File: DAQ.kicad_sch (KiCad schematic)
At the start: 6 parts, among them IC1 ABX00053, IC2 TEENSY_4.1

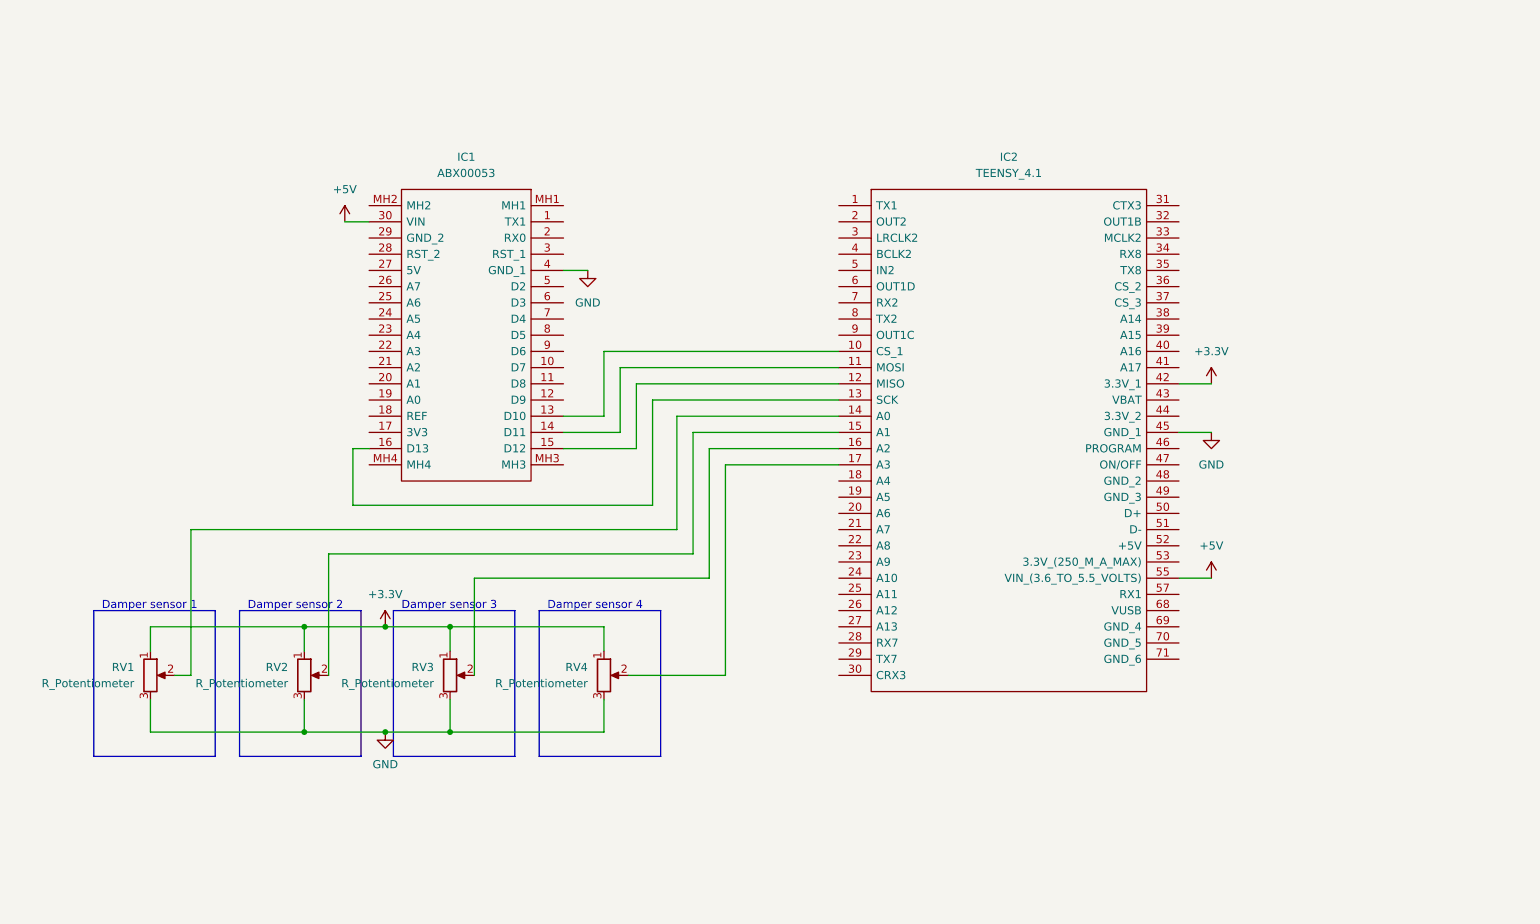
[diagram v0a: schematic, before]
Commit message: added wheel speed sensors connection
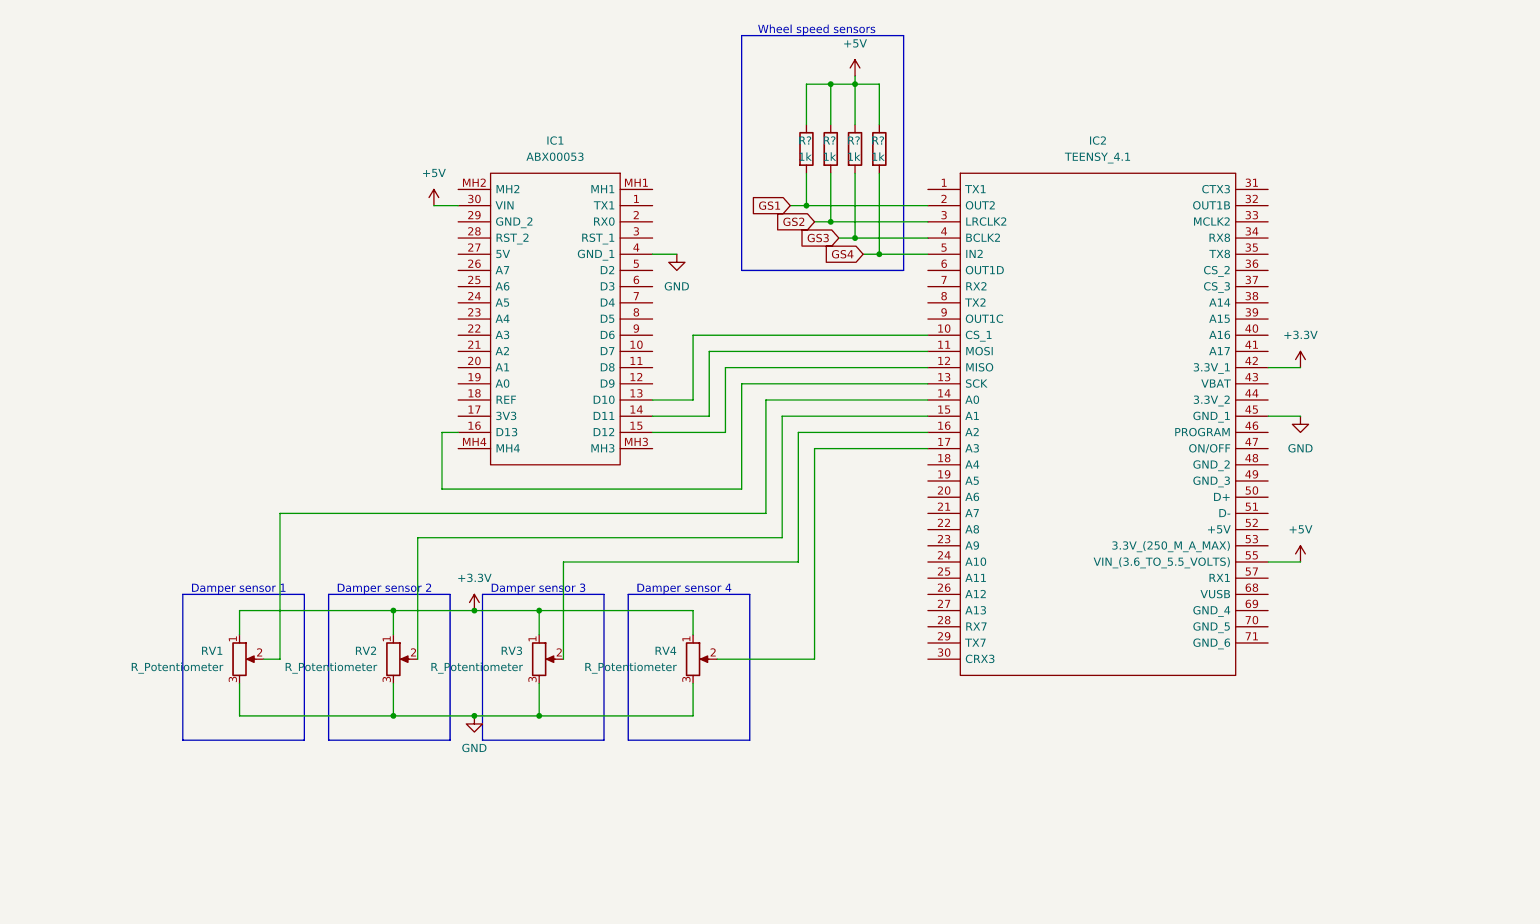
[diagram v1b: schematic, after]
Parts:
- added R? (x4): 1k, symbol Device:R
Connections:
- net +5V: now also R?.1, R?.1, R?.1, R?.1
- net GS1: now reaches IC2.2 (OUT2)
- net GS1: now also R?.2
- net GS2: now reaches IC2.3 (LRCLK2)
- net GS2: now also R?.2
- net GS3: now reaches IC2.4 (BCLK2)
- net GS3: now also R?.2
- net GS4: now reaches IC2.5 (IN2)
- net GS4: now also R?.2
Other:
- note added: "Wheel speed sensors"
- moved on the sheet: IC1, IC2, RV1, RV2, RV3, RV4

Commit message: added battery voltage sensor and steering wheel sensor
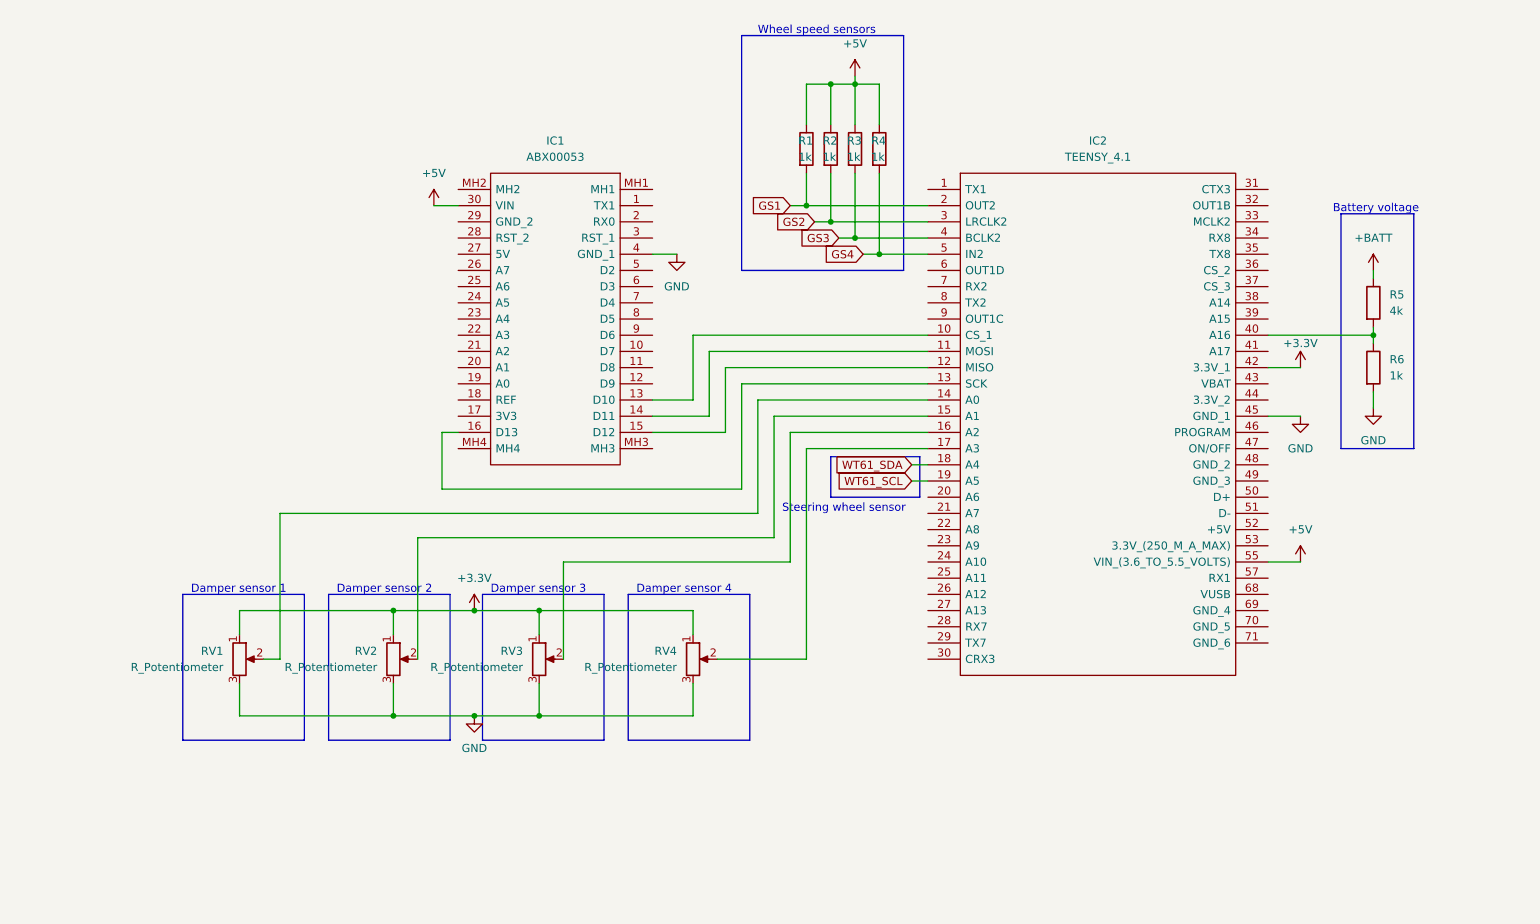
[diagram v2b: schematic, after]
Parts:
- added R5: 4k, symbol Device:R
- added R6: 1k, symbol Device:R
- gave numbers to parts that had none: 4
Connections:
- net GND: now also R6.2
- net WT61_SDA: now reaches IC2.18 (A4)
- net WT61_SCL: now reaches IC2.19 (A5)
- net at IC2.40 (A16): now also R5.2, R6.1
- new net +BATT: R5.1
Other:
- note added: "Battery voltage"
- note added: "Steering wheel sensor"

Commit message: new sensors
zener diode to hall effect input; coin cell for teensy RTC
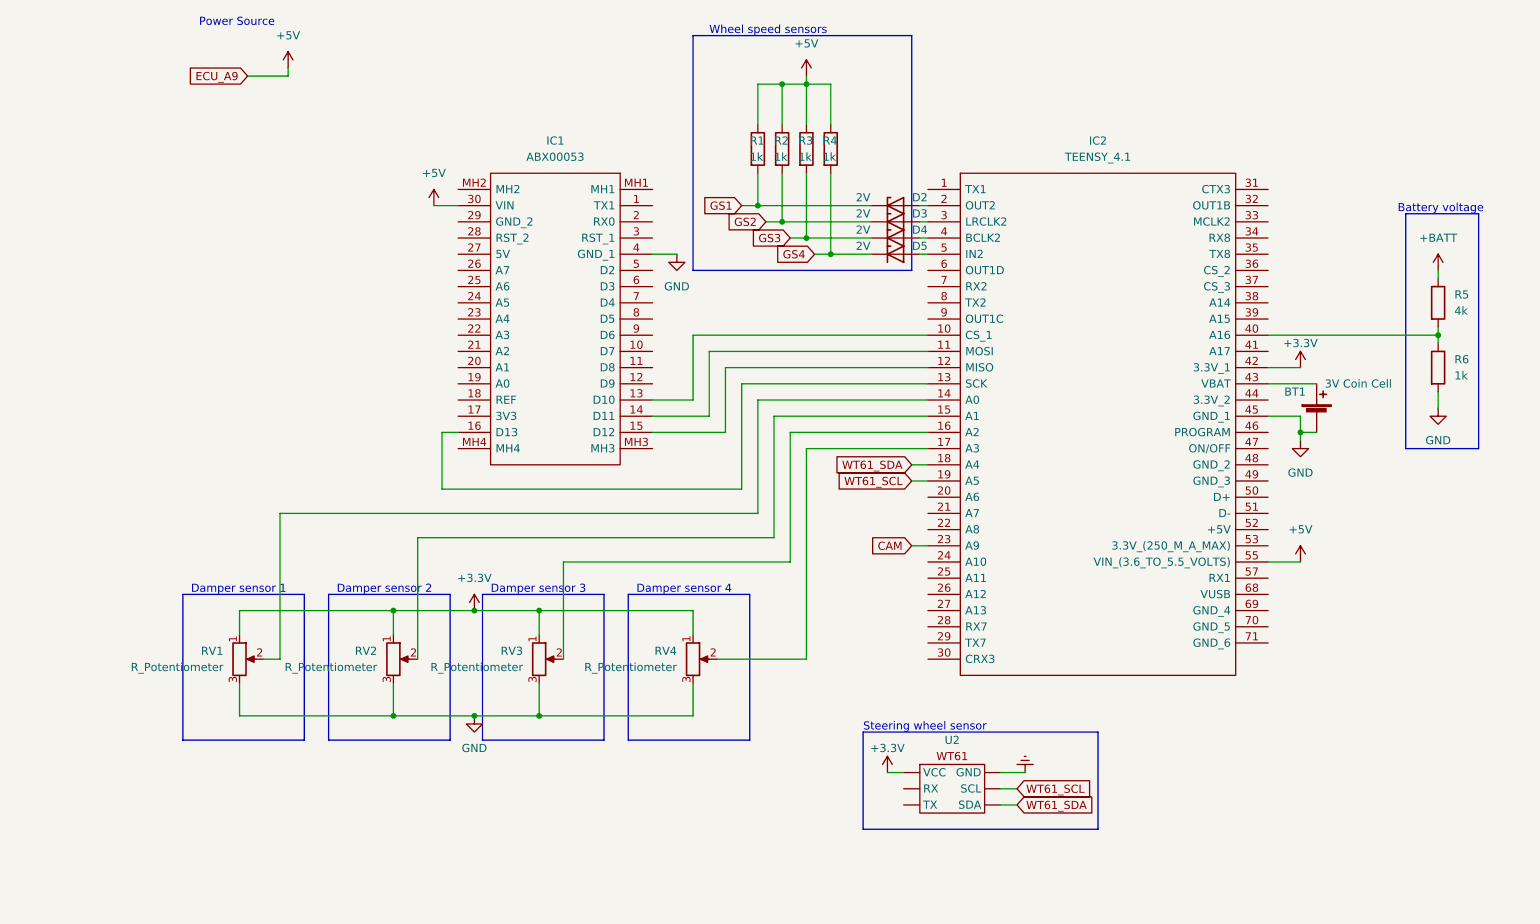
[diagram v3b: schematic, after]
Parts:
- added BT1: 3V Coin Cell, symbol Device:Battery_Cell
- added D2, D3, D4, D5: 2V, symbol Device:D_Zener
- added U2: ~, symbol Sensor:WT61
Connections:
- net +3.3V: now also U2. (VCC)
- net GND: now also BT1.2 (-)
- net GS1: now also D2.1 (K); no longer IC2.2 (OUT2)
- net GS2: now also D3.1 (K); no longer IC2.3 (LRCLK2)
- net GS3: now also D4.1 (K); no longer IC2.4 (BCLK2)
- net GS4: now also D5.1 (K); no longer IC2.5 (IN2)
- net WT61_SCL: now also U2. (VCC)
- net WT61_SDA: now also U2. (VCC)
- net CAM: now reaches IC2.23 (A9)
- net at IC2.43 (VBAT): now also BT1.1 (+)
- new net: D2.2 (A), IC2.2 (OUT2)
- new net: D3.2 (A), IC2.3 (LRCLK2)
- new net: D5.2 (A), IC2.5 (IN2)
- new net: D4.2 (A), IC2.4 (BCLK2)
- new net Earth: U2. (VCC)
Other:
- note added: "Power Source"
- moved on the sheet: R1, R2, R3, R4, R5, R6

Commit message: Update DAQ.kicad_sch
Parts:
- removed IC1: ABX00053, ABX00053, symbol SamacSys_Parts:ABX00053
- added D1: 5V, symbol Device:D_Zener
- added FB1: FerriteBead, symbol Device:FerriteBead
- added R10, R11, R12, R13, R14, R9: 1k, symbol Device:R
- added R7, R8: 470, symbol Device:R
- added RV5: R_Potentiometer, symbol Device:R_Potentiometer
- added U1: ~, symbol Sensor:WT61
- added U3: CD-PA1616D, XCVR_CD-PA1616D, symbol CD-PA1616D:CD-PA1616D
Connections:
- net Earth is gone; now on net S_SDA: U2. (VCC)
- net WT61_SDA is gone; now on net S_SDA: IC2.18 (A4), U2. (VCC)
- net +3.3V: now also FB1.1, R10.1, R11.1, R12.1, R13.1, R14.1, R9.1, U1. (VCC)
- net CAM: now also D1.1 (K); no longer IC2.23 (A9)
- net GND: now also U2. (VCC), RV5.3, U1. (VCC), U3.12 (GND), U3.19 (GND), U3.3 (GND), U3.8 (GND)
- net +3V0: now reaches BT1.1 (+), IC2.43 (VBAT)
- net +3V0: now also U3.4 (VBACKUP)
- net at RV3.2: now also IC2.20 (A6); no longer IC2.16 (A2)
- net at RV4.2: now also IC2.21 (A7); no longer IC2.17 (A3)
- net at IC2.22 (A8): now also D1.2 (A)
- net GPS_SCL: now reaches IC2.24 (A10)
- net GPS_SCL: now also R10.2, U3.14 (RX1/I2C_SCL)
- net GPS_SDA: now reaches IC2.25 (A11)
- net GPS_SDA: now also R9.2, U3.15 (TX1/I2C_SDA)
- net at IC2.26 (A12): now also RV5.2
- net at IC2.7 (RX2): now also R7.2
- net at IC2.8 (TX2): now also R8.2
- net S_SDA: now reaches U2. (VCC)
- net S_SDA: now also R14.2
- net WT61_SCL renamed S_SCL
- net S_SCL: now also R13.2
- new net: FB1.2, U3.1 (VCC)
- new net: R8.1, U3.10 (RX)
- new net: U3.16 (NC), U3.17 (NC), U3.18 (NC), U3.20 (NC), U3.6 (NC), U3.7 (NC)
- new net: R7.1, U3.9 (TX)
- new net W_SCL: IC2.16 (A2), R11.2, U1. (VCC)
- new net W_SDA: IC2.17 (A3), R12.2, U1. (VCC)
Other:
- note added: "Throttle position"
- note added: "Whole car gyroscope/accelerometer"
- moved on the sheet: BT1, RV1, RV2, RV3, RV4, U2

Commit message: Update DAQ.kicad_sch
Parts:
- added SW1, SW2: SW_Push_Open, symbol Switch:SW_Push_Open
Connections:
- net GND: now also SW1.2 (B), SW2.2 (B)
- net at IC2.31 (CTX3): now also SW1.1 (A)
- net at IC2.32 (OUT1B): now also SW2.1 (A)
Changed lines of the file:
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@@
   (junction (at 57.15 132.08) (diameter 0) (color 0 0 0 0)
   )
+  (junction (at 223.52 63.5) (diameter 0) (color 0 0 0 0)
+  )
   (junction (at 80.01 148.59) (diameter 0) (color 0 0 0 0)
   )
@@
     (stroke (width 0) (type default))
   )
+  (wire (pts (xy 219.71 60.96) (xy 223.52 60.96))
+    (stroke (width 0) (type default))
+  )
   (wire (pts (xy 104.14 132.08) (xy 80.01 132.08))
     (stroke (width 0) (type default))
@@
     (stroke (width 0) (type default))
   )
+  (wire (pts (xy 223.52 60.96) (xy 223.52 63.5))
+    (stroke (width 0) (type default))
+  )
   (wire (pts (xy 129.54 44.45) (xy 129.54 50.8))
     (stroke (width 0) (type default))
@@
     (stroke (width 0) (type default))
   )
+  (wire (pts (xy 205.74 63.5) (xy 209.55 63.5))
+    (stroke (width 0) (type default))
+  )
   (wire (pts (xy 33.02 132.08) (xy 33.02 135.89))
     (stroke (width 0) (type default))
@@
     (stroke (width 0) (type default))
   )
+  (wire (pts (xy 205.74 60.96) (xy 209.55 60.96))
+    (stroke (width 0) (type default))
+  )
   (polyline (pts (xy 113.03 152.4) (xy 93.98 152.4))
     (stroke (width 0) (type default))
@@
   )
   (polyline (pts (xy 137.16 129.54) (xy 137.16 152.4))
+    (stroke (width 0) (type default))
+  )
+  (wire (pts (xy 219.71 63.5) (xy 223.52 63.5))
     (stroke (width 0) (type default))
   )
@@
     )
   )
+  (symbol (lib_id "Switch:SW_Push_Open") (at 214.63 60.96 0) (unit 1)
+    (in_bom yes) (on_board yes) (dnp no) (fields_autoplaced)
+    (property "Reference" "SW1" (at 214.63 55.88 0)
+      (effects (font (size 1.27 1.27)))
+    )
+    (property "Value" "SW_Push_Open" (at 214.63 58.42 0)
+      (effects (font (size 1.27 1.27)))
+    )
+    (property "Footprint" "" (at 214.63 55.88 0)
+      (effects (font (size 1.27 1.27)) hide)
+    )
+    (property "Datasheet" "~" (at 214.63 55.88 0)
+      (effects (font (size 1.27 1.27)) hide)
+    )
+    (pin "1")
+    (pin "2")
+    (instances
+      (project "DAQ"
+        (path "/813e588e-265c-47f4-92de-e30a6c3791f8"
+          (reference "SW1") (unit 1)
+        )
+      )
+    )
+  )
   (symbol (lib_id "power:+3.3V") (at 154.94 151.13 0) (unit 1)
     (in_bom yes) (on_board yes) (dnp no)
@@
         (path "/813e588e-265c-47f4-92de-e30a6c3791f8"
           (reference "#PWR06") (unit 1)
+        )
+      )
+    )
+  )
+  (symbol (lib_id "Switch:SW_Push_Open") (at 214.63 63.5 0) (unit 1)
+    (in_bom yes) (on_board yes) (dnp no)
+    (property "Reference" "SW2" (at 214.63 66.04 0)
+      (effects (font (size 1.27 1.27)))
+    )
+    (property "Value" "SW_Push_Open" (at 215.9 68.58 0)
+      (effects (font (size 1.27 1.27)))
+    )
+    (property "Footprint" "" (at 214.63 58.42 0)
+      (effects (font (size 1.27 1.27)) hide)
+    )
+    (property "Datasheet" "~" (at 214.63 58.42 0)
+      (effects (font (size 1.27 1.27)) hide)
+    )
+    (pin "1")
+    (pin "2")
+    (instances
+      (project "DAQ"
+        (path "/813e588e-265c-47f4-92de-e30a6c3791f8"
+          (reference "SW2") (unit 1)
         )
       )
@@
         )
       )
+    )
+  )
+  (symbol (lib_id "power:GND") (at 223.52 63.5 0) (unit 1)
+    (in_bom yes) (on_board yes) (dnp no) (fields_autoplaced)
+    (property "Reference" "#PWR014" (at 223.52 69.85 0)
+      (effects (font (size 1.27 1.27)) hide)
+    )
+    (property "Value" "GND" (at 223.52 68.58 0)
+      (effects (font (size 1.27 1.27)))
+    )
+    (property "Footprint" "" (at 223.52 63.5 0)
+      (effects (font (size 1.27 1.27)) hide)
+    )
+    (property "Datasheet" "" (at 223.52 63.5 0)
+      (effects (font (size 1.27 1.27)) hide)
+    )
+    (pin "1")
+    (instances
+      (project "DAQ"
+        (path "/813e588e-265c-47f4-92de-e30a6c3791f8"
+          (reference "#PWR014") (unit 1)
+        )
+      )
